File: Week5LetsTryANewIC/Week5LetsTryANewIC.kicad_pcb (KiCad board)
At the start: 2 copper layers, 17 x 28 mm, 10 parts, among them J1 Conn_01x09_Male, U1 BMA400

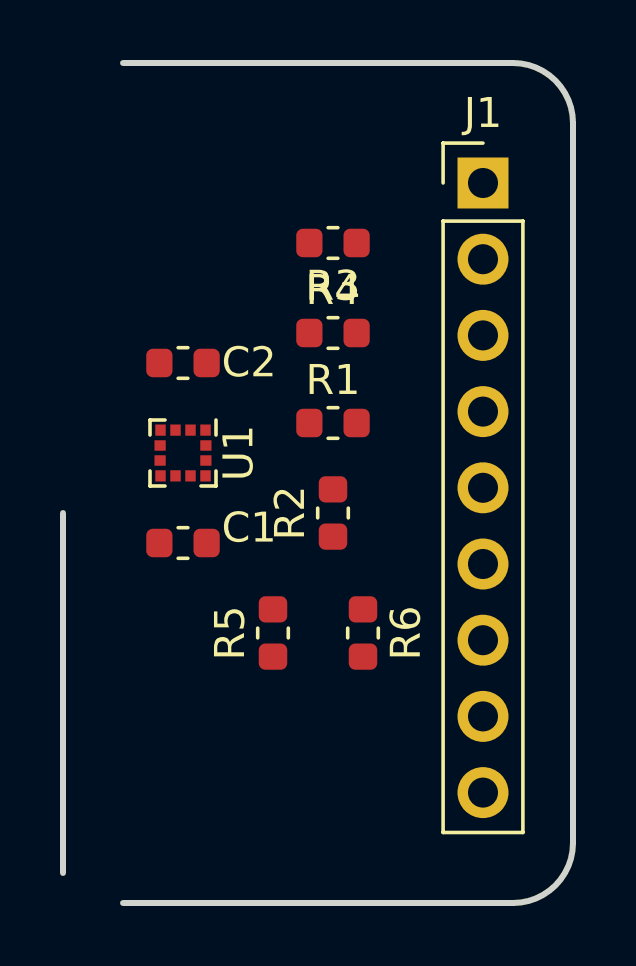
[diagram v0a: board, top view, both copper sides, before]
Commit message: week 5 routing complete
silk and artwork still required
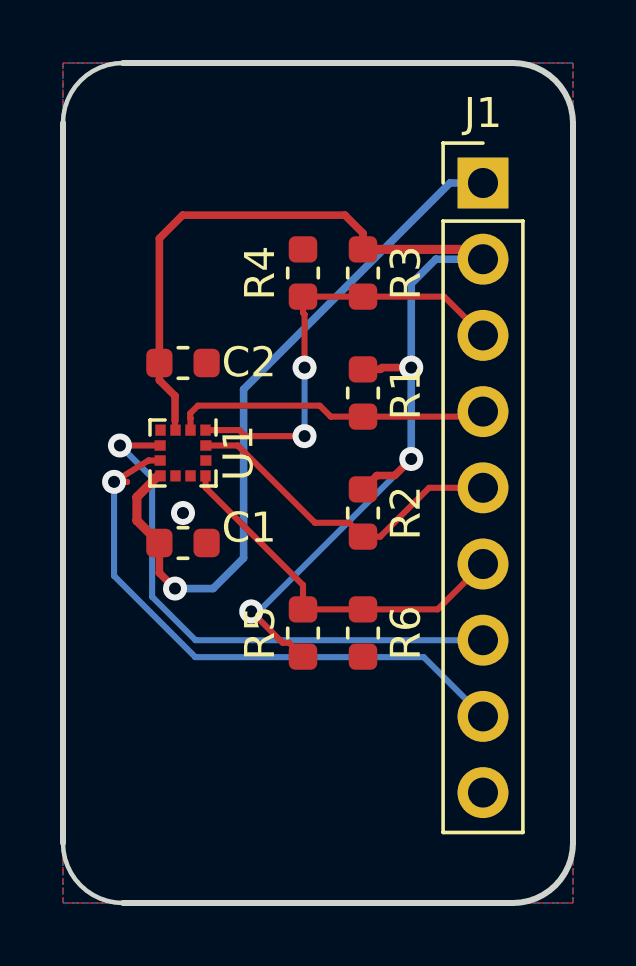
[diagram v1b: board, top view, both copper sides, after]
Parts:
- moved R4 2.24 mm to (162.0, 70.0), turned to 90 degrees
- moved R1 1.41 mm to (164.0, 74.0), turned to 270 degrees
- moved R3 1.41 mm to (164.0, 70.0), turned to 270 degrees
- moved R2 1.00 mm to (164.0, 78.0), turned to 270 degrees
- moved R5 1.00 mm to (162.0, 82.0)
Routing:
- net VDDA: track 0.00 -> 40.7 mm, vias 0 -> 3
- net VDD: track 0.00 -> 23.8 mm, vias 0 -> 1
- net /INT2: track 0.00 -> 20.0 mm, vias 0 -> 1
- net /INT1: track 0.00 -> 18.7 mm, vias 0 -> 1
- net /SDA: track 0.00 -> 14.6 mm, vias 0 -> 2
- net /CSB: track 0.00 -> 12.4 mm
- net /SCX: track 0.00 -> 11.2 mm
- net /SDX: track 0.00 -> 10.6 mm
- net GND: vias 0 -> 1
- added copper zone on B.Cu, net GND
- added copper zone on F.Cu, net GND
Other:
- outline, holes or cut-outs redrawn
- net class Power: trace_width 0.3048 -> 0.2032
